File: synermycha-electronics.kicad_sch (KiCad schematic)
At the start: 0 parts

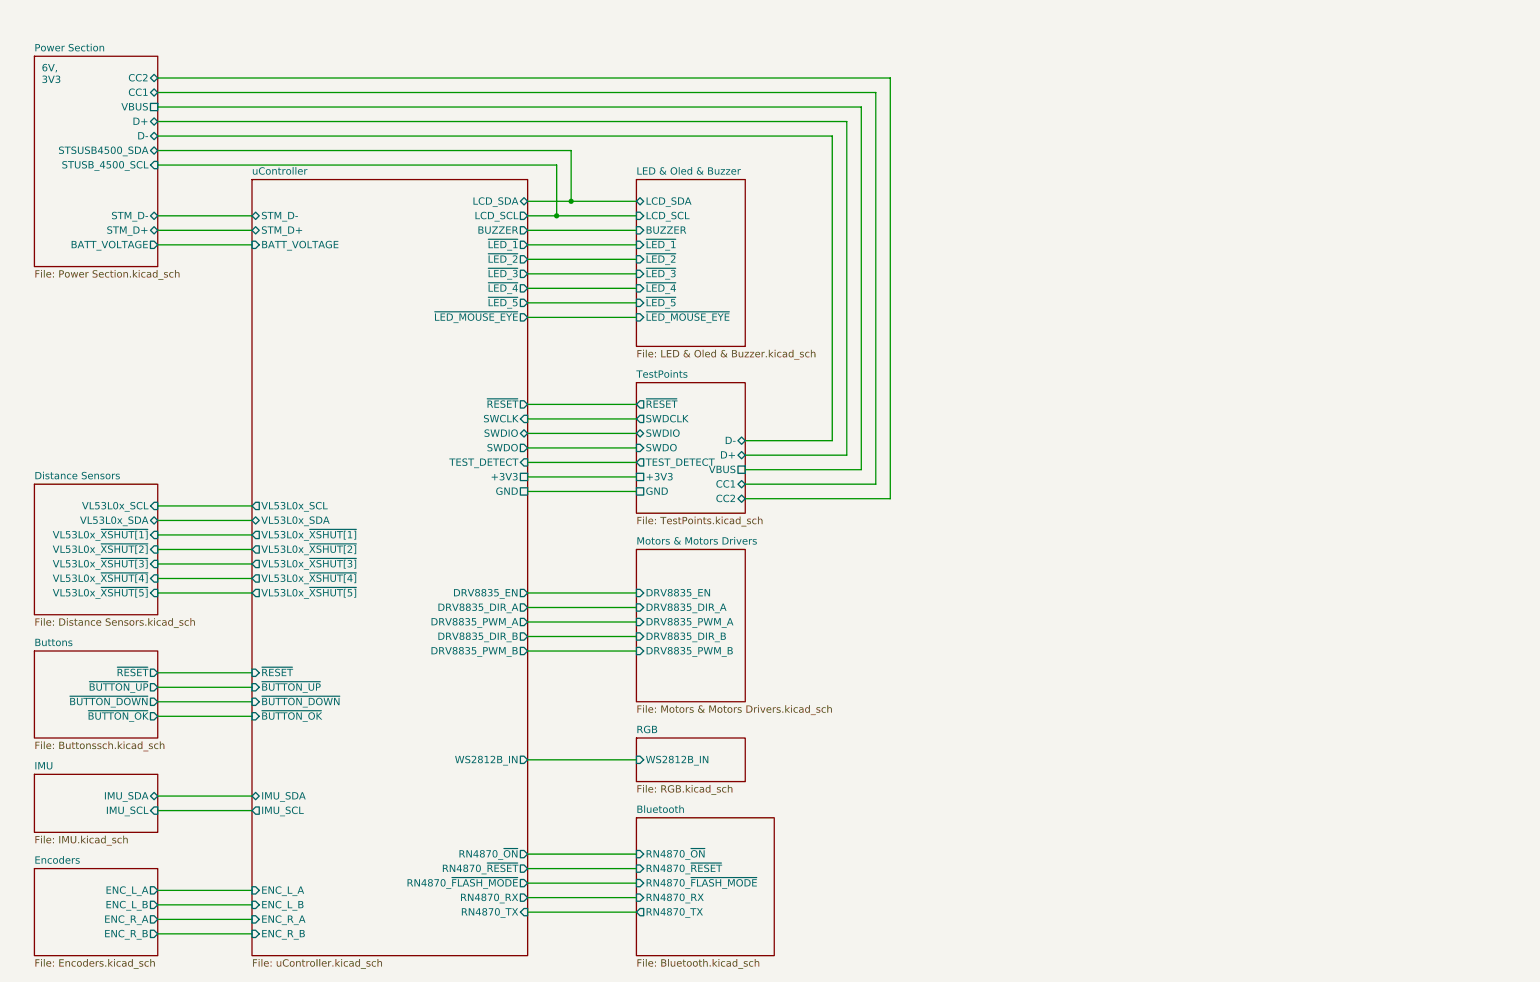
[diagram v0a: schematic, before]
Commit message: Update subsheet names
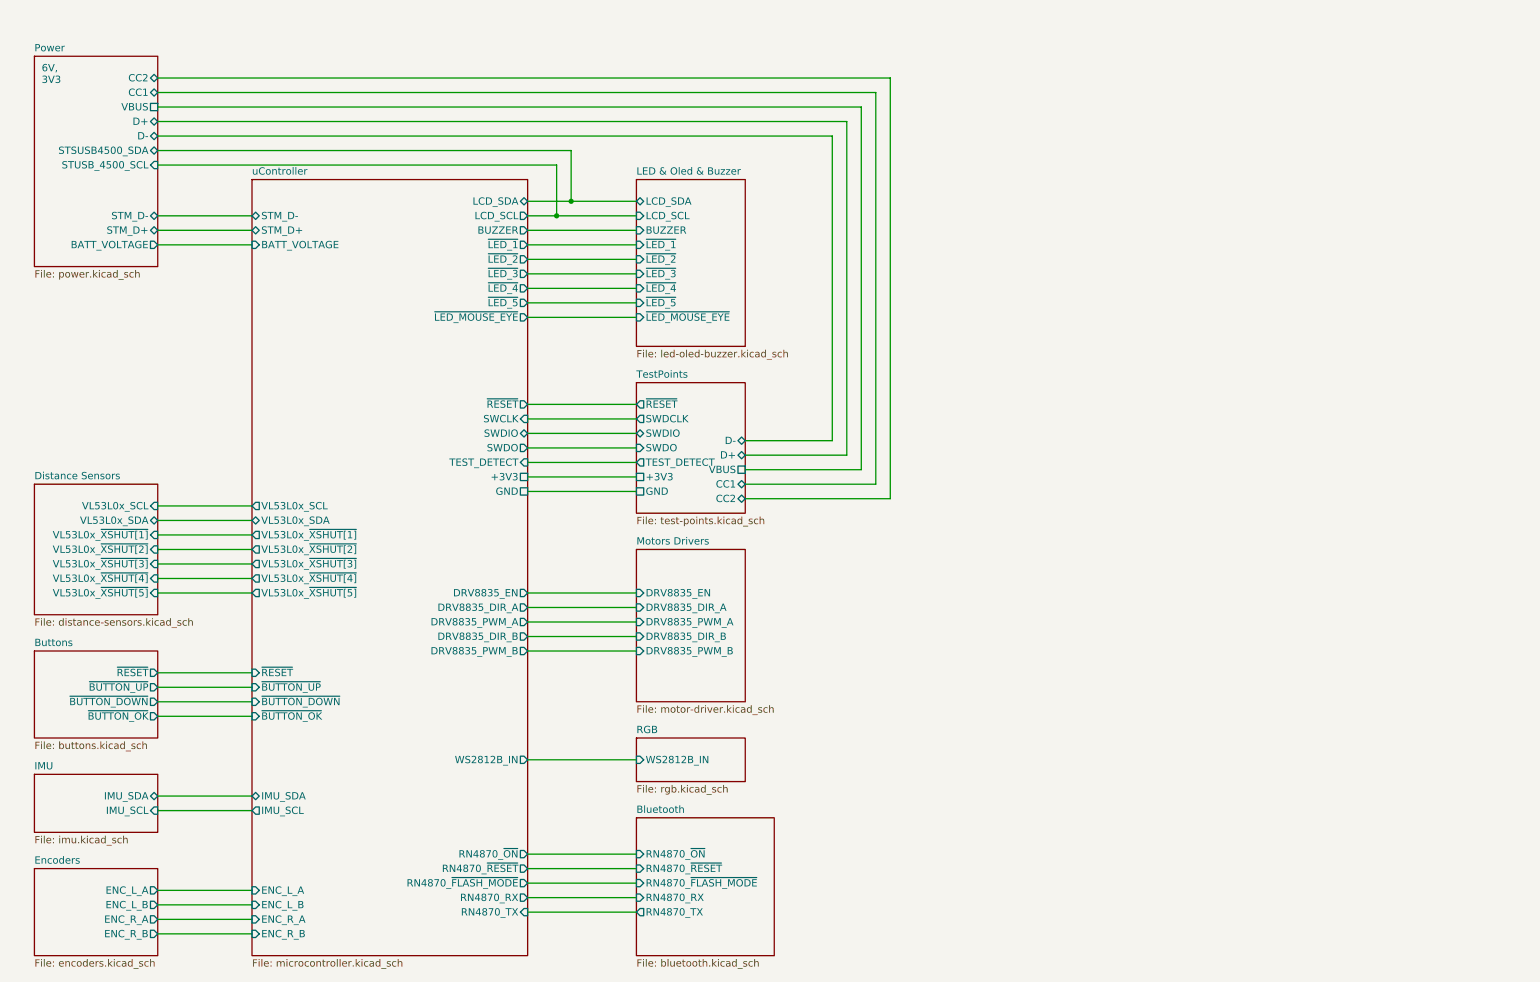
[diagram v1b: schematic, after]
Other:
- sheet Motors & Motors Drivers renamed Motors Drivers
- sheet Power Section renamed Power
- sheet Bluetooth: file Bluetooth.kicad_sch -> bluetooth.kicad_sch
- sheet Buttons: file Buttonssch.kicad_sch -> buttons.kicad_sch
- sheet Distance Sensors: file Distance Sensors.kicad_sch -> distance-sensors.kicad_sch
- sheet Encoders: file Encoders.kicad_sch -> encoders.kicad_sch
- sheet IMU: file IMU.kicad_sch -> imu.kicad_sch
- sheet LED & Oled & Buzzer: file LED & Oled & Buzzer.kicad_sch -> led-oled-buzzer.kicad_sch
- sheet Motors Drivers: file Motors & Motors Drivers.kicad_sch -> motor-driver.kicad_sch
- sheet Power: file Power Section.kicad_sch -> power.kicad_sch
- sheet RGB: file RGB.kicad_sch -> rgb.kicad_sch
- sheet TestPoints: file TestPoints.kicad_sch -> test-points.kicad_sch
- sheet uController: file uController.kicad_sch -> microcontroller.kicad_sch

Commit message: Add bus to the motor controller
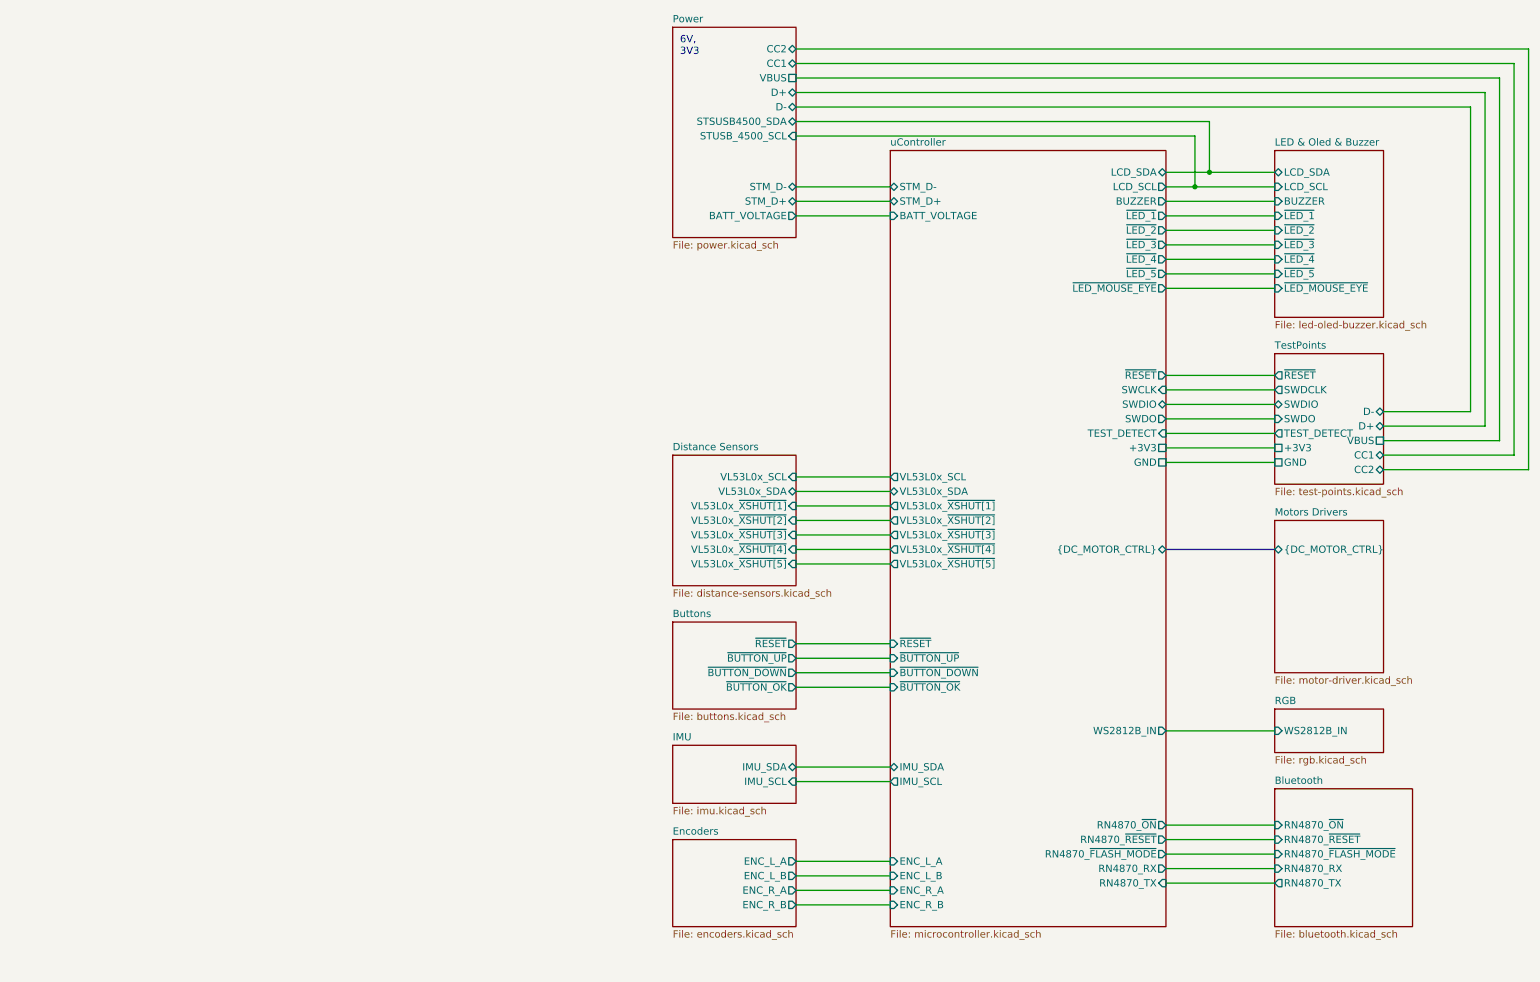
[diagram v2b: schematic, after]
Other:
- sheet Motors Drivers ports: added {DC_MOTOR_CTRL}; removed DRV8835_DIR_A, DRV8835_DIR_B, DRV8835_EN, DRV8835_PWM_A, DRV8835_PWM_B
- sheet uController ports: added {DC_MOTOR_CTRL}; removed DRV8835_DIR_A, DRV8835_DIR_B, DRV8835_EN, DRV8835_PWM_A, DRV8835_PWM_B

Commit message: Update root sheet
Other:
- sheet Bluetooth ports: added none; removed RN4870_RX, RN4870_TX, RN4870_~{FLASH_MODE}, RN4870_~{ON}, RN4870_~{RESET}
- sheet Buttons ports: added JOY{JOY}; removed ~{BUTTON_DOWN}, ~{BUTTON_OK}, ~{BUTTON_UP}, ~{RESET}
- sheet Distance Sensors ports: added VL53L0x_~{XSHUT[1..5]}, VL53L0x{I2C}; removed VL53L0x_SCL, VL53L0x_SDA, VL53L0x_~{XSHUT[1]}, VL53L0x_~{XSHUT[2]}, VL53L0x_~{XSHUT[3]}, VL53L0x_~{XSHUT[4]}, VL53L0x_~{XSHUT[5]}
- sheet Encoders ports: added ENC_L{ENC}, ENC_R{ENC}; removed ENC_L_A, ENC_L_B, ENC_R_A, ENC_R_B
- sheet IMU ports: added IMU{I2C}; removed IMU_SCL, IMU_SDA
- sheet LED & Oled & Buzzer ports: added {~{LED_[1..5]} ~{LED_EYE}}; removed ~{LED_1}, ~{LED_2}, ~{LED_3}, ~{LED_4}, ~{LED_5}, ~{LED_MOUSE_EYE}
- sheet Power ports: added none; removed CC1, CC2, D+, D-, STM_D+, STM_D-, STSUSB4500_SDA, STUSB_4500_SCL, VBUS
- sheet TestPoints ports: added none; removed +3V3, CC1, CC2, D+, D-, GND, SWDCLK, SWDIO, SWDO, TEST_DETECT, VBUS, ~{RESET}
- sheet uController ports: added DC_MOTOR{DC_MOTOR_CTRL}, ENC_L{ENC}, ENC_R{ENC}, IMU{I2C}, JOY{JOY}, SD{SDIO}, VL53L0x_~{XSHUT[1..5]}, VL53L0x{I2C}, {~{LED_[1..5]} ~{LED_EYE}}; removed +3V3, ENC_L_A, ENC_L_B, ENC_R_A, ENC_R_B, GND, IMU_SCL, IMU_SDA, RN4870_RX, RN4870_TX, RN4870_~{FLASH_MODE}, RN4870_~{ON}, RN4870_~{RESET}, STM_D+, STM_D-, SWCLK, SWDIO, SWDO, TEST_DETECT, VL53L0x_SCL, VL53L0x_SDA, VL53L0x_~{XSHUT[1]}, VL53L0x_~{XSHUT[2]}, VL53L0x_~{XSHUT[3]}, VL53L0x_~{XSHUT[4]}, VL53L0x_~{XSHUT[5]}, {DC_MOTOR_CTRL}, ~{BUTTON_DOWN}, ~{BUTTON_OK}, ~{BUTTON_UP}, ~{LED_1}, ~{LED_2}, ~{LED_3}, ~{LED_4}, ~{LED_5}, ~{LED_MOUSE_EYE}, ~{RESET}

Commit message: Remove VLX wiring
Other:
- sheet Distance Sensors ports: added none; removed VL53L0x_~{XSHUT[1..5]}, VL53L0x{I2C}
- sheet uController ports: added none; removed SD{SDIO}, VL53L0x_~{XSHUT[1..5]}, VL53L0x{I2C}
